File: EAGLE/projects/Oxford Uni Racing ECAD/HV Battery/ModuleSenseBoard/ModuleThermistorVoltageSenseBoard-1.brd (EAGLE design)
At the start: 126.4 x 93.8 mm, 12 parts

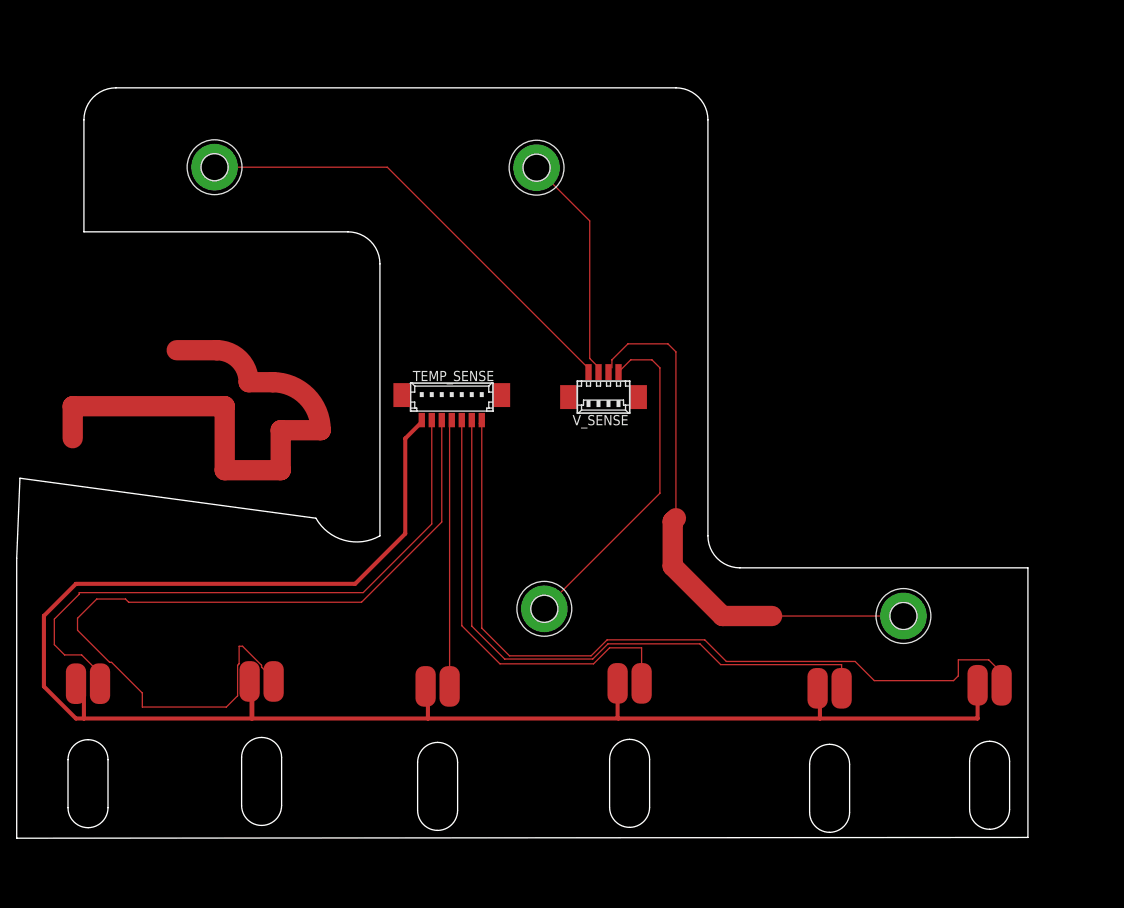
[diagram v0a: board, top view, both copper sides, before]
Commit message: updated thermister footprint
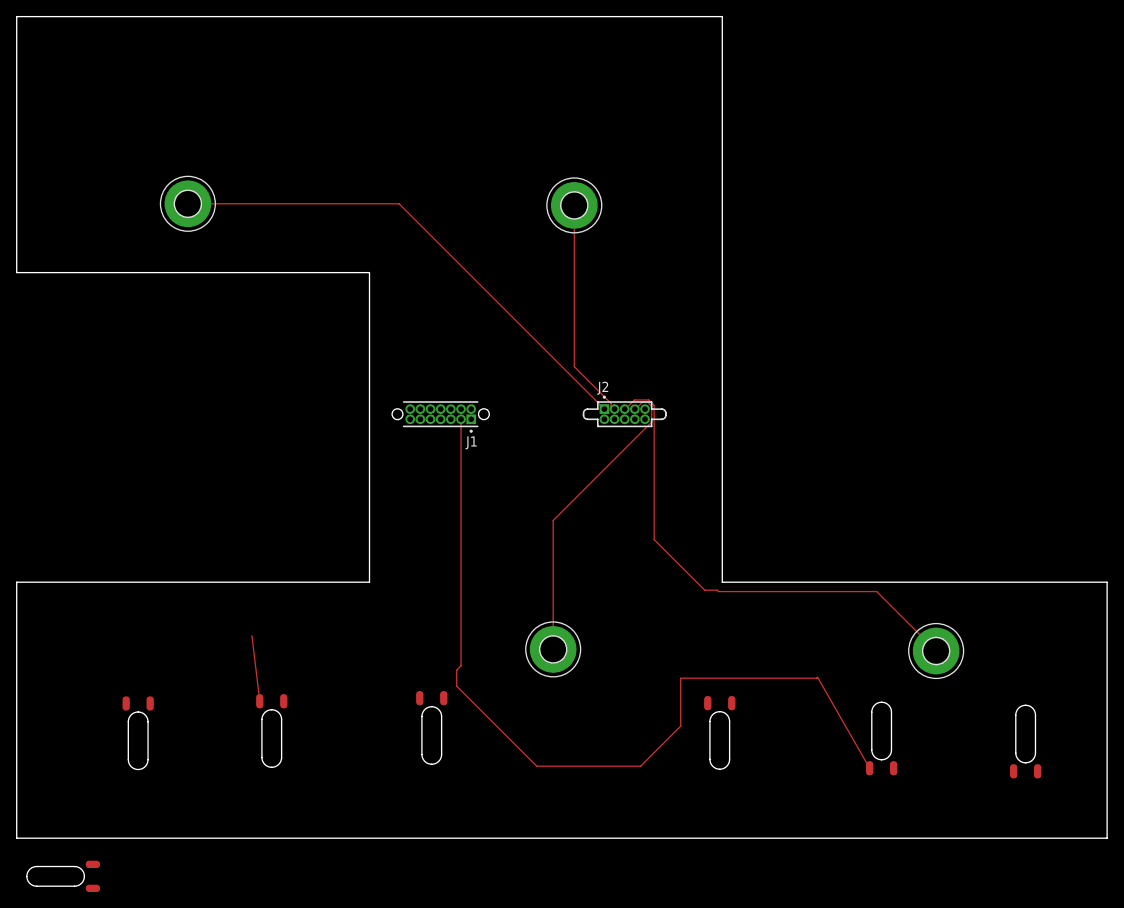
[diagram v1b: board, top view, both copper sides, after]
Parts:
- removed TEMP_SENSE: 53398-07, con-molex:53398-07
- removed V_SENSE: 53261-04, con-molex:53261-04
- added J1: SFML-107-01-L-D-A, SFML-107-01-L-D-A:SAMTEC_SFML-107-01-L-D-A
- added J2: SFML-105-01-L-D, SFML-105-01-L-D:SAMTEC_SFML-105-01-L-D
- added T7: (no value), Thermistor:THERMISTOR_CUTOUT
- moved T2 17.7 mm to (106.9, 18.3), turned to 270 degrees
- moved T1 16.8 mm to (124.9, 17.9), turned to 270 degrees
- moved T3 11.7 mm to (89.1, 7.36)
- moved T6 7.81 mm to (16.4, 7.32)
- moved T4 7.28 mm to (53.1, 7.98)
- moved V1+ 6.67 mm to (69.7, 79.1)
- moved T5 6.00 mm to (33.1, 7.60)
- moved V2+ 5.99 mm to (114.9, 23.4)
- moved V1- 5.66 mm to (21.4, 79.3)
- moved V3+ 5.19 mm to (67.1, 23.6)
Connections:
- removed net N$5: T4.2, TEMP_SENSE.4
- removed net N$6: T5.2, TEMP_SENSE.5
- new net N$1: J1.07, T4.2
- new net N$2: J1.09, T5.2
- net GND: now also J1.13; no longer TEMP_SENSE.7
- net N$3: now also J1.03; no longer TEMP_SENSE.2
- net N$4: now also J1.05; no longer TEMP_SENSE.3
- net N$7: now also J1.11; no longer TEMP_SENSE.6
- net TSENSE1: now also J1.01; no longer TEMP_SENSE.1
- net V1+: now also J2.03; no longer V_SENSE.2
- net V1-: now also J2.01; no longer V_SENSE.1
- net V2+: now also J2.05; no longer V_SENSE.3
- net V3+: now also J2.07; no longer V_SENSE.4
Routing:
- net GND: track 217.8 -> 8.24 mm
- net N$6: track 103.8 -> 0.00 mm
- net TSENSE1: track 101.2 -> 0.00 mm
- net N$7: track 76.9 -> 0.00 mm
- net N$1: track 70.1 -> 0.00 mm
- net N$4: track 55.4 -> 0.00 mm
- net N$5: track 33.4 -> 0.00 mm
- net N$3: track 79.5 -> 104.1 mm
- net V2+: track 68.6 -> 62.2 mm
- net V1-: track 57.1 -> 62.7 mm
- net V3+: track 42.3 -> 38.1 mm
- net V1+: track 28.8 -> 27.5 mm
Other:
- board size 126.4 x 93.8 mm -> 136.3 x 102.7 mm
- board text added: "TS"
- board text added: "lv"

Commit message: New pcb board designed to work with countersink bus bar.
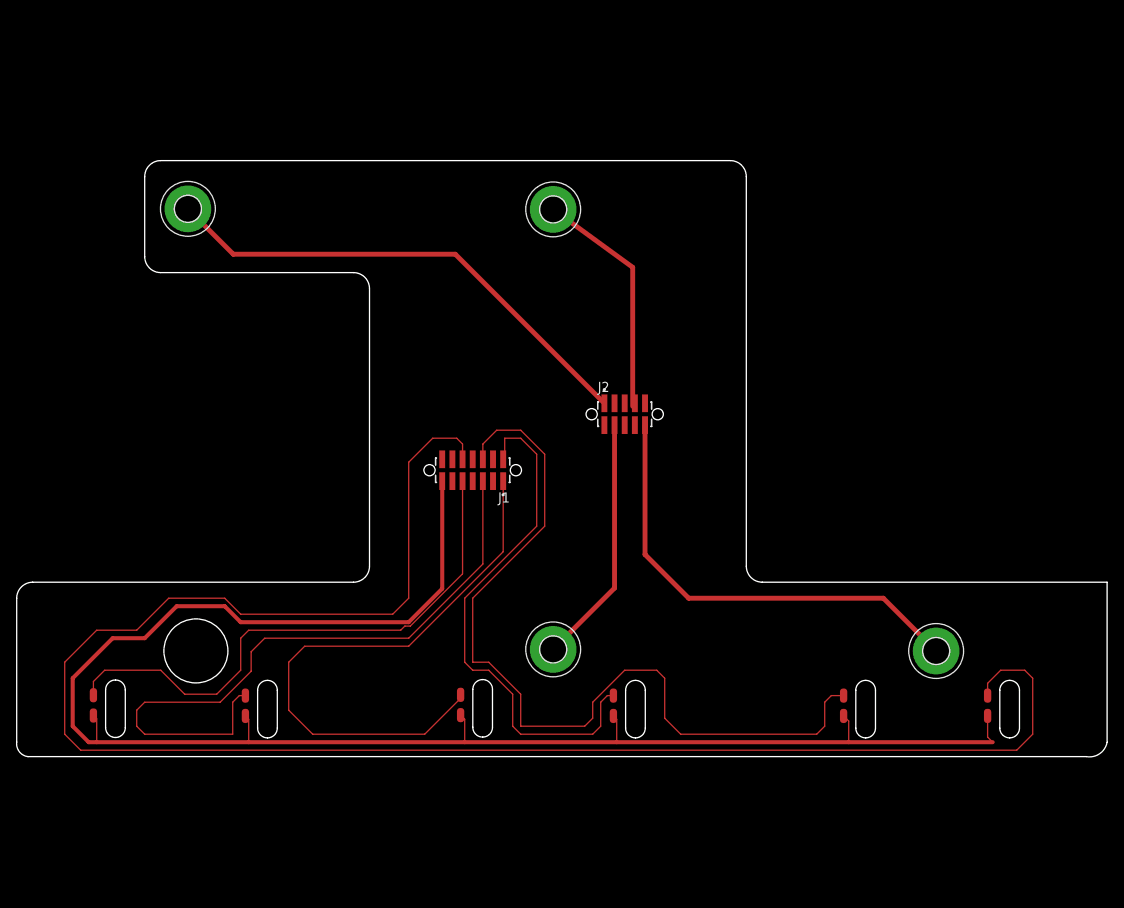
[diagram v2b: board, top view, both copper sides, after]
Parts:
- removed T7: (no value), Thermistor:THERMISTOR_CUTOUT
- J1: value SFML-107-01-L-D-A -> SFML-107-02-L-D-A; device SFML-107-01-L-D-A:SAMTEC_SFML-107-01-L-D-A -> SFML-107-02-L-D-A:SAMTEC_SFML-107-02-L-D-A
- J2: value SFML-105-01-L-D -> SFML-105-02-L-D-A; device SFML-105-01-L-D:SAMTEC_SFML-105-01-L-D -> SFML-105-02-L-D-A:SAMTEC_SFML-105-02-L-D-A
- moved T3 18.8 mm to (76.1, 21.0), turned to 270 degrees
- moved T6 14.7 mm to (11.1, 21.1), turned to 270 degrees
- moved T5 13.7 mm to (30.1, 21.0), turned to 270 degrees
- moved T4 13.7 mm to (57.0, 21.1), turned to 270 degrees
- moved J1 8.06 mm to (57.0, 46.0)
- moved T1 3.70 mm to (122.9, 21.0)
- moved T2 3.39 mm to (104.9, 21.0)
- moved V1+ 2.69 mm to (67.1, 78.6)
- moved V1- 0.63 mm to (21.4, 78.7)
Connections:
- removed net N$7: J1.11, T6.2
- removed net TSENSE1: J1.01, T1.2
- new net N$5: J1.06, T2.2
- new net N$6: J1.10, T1.2
- net N$1: now also J1.05, T5.2; no longer J1.07, T4.2
- net N$2: now also T6.2; no longer T5.2
- net N$3: now also J1.01, T4.2; no longer J1.03, T2.2
- net N$4: now also J1.02; no longer J1.05
- net V1+: now also J2.07; no longer J2.03
- net V2+: now also J2.10; no longer J2.05
- net V3+: now also J2.04; no longer J2.07
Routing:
- net N$6: track 0.00 -> 222.1 mm
- net GND: track 8.24 -> 209.7 mm
- net N$5: track 0.00 -> 107.8 mm
- net N$1: track 0.00 -> 83.0 mm
- net N$2: track 0.00 -> 69.8 mm
- net N$4: track 0.00 -> 65.7 mm
- net N$3: track 104.1 -> 72.4 mm
- net V3+: track 38.1 -> 31.2 mm
- net V2+: track 62.2 -> 57.6 mm
- net V1+: track 27.5 -> 29.7 mm
- net V1-: track 62.7 -> 62.1 mm
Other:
- board size 136.3 x 102.7 mm -> 136.3 x 74.5 mm
